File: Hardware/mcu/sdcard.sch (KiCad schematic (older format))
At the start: 2 parts, among them U801 MICROSD

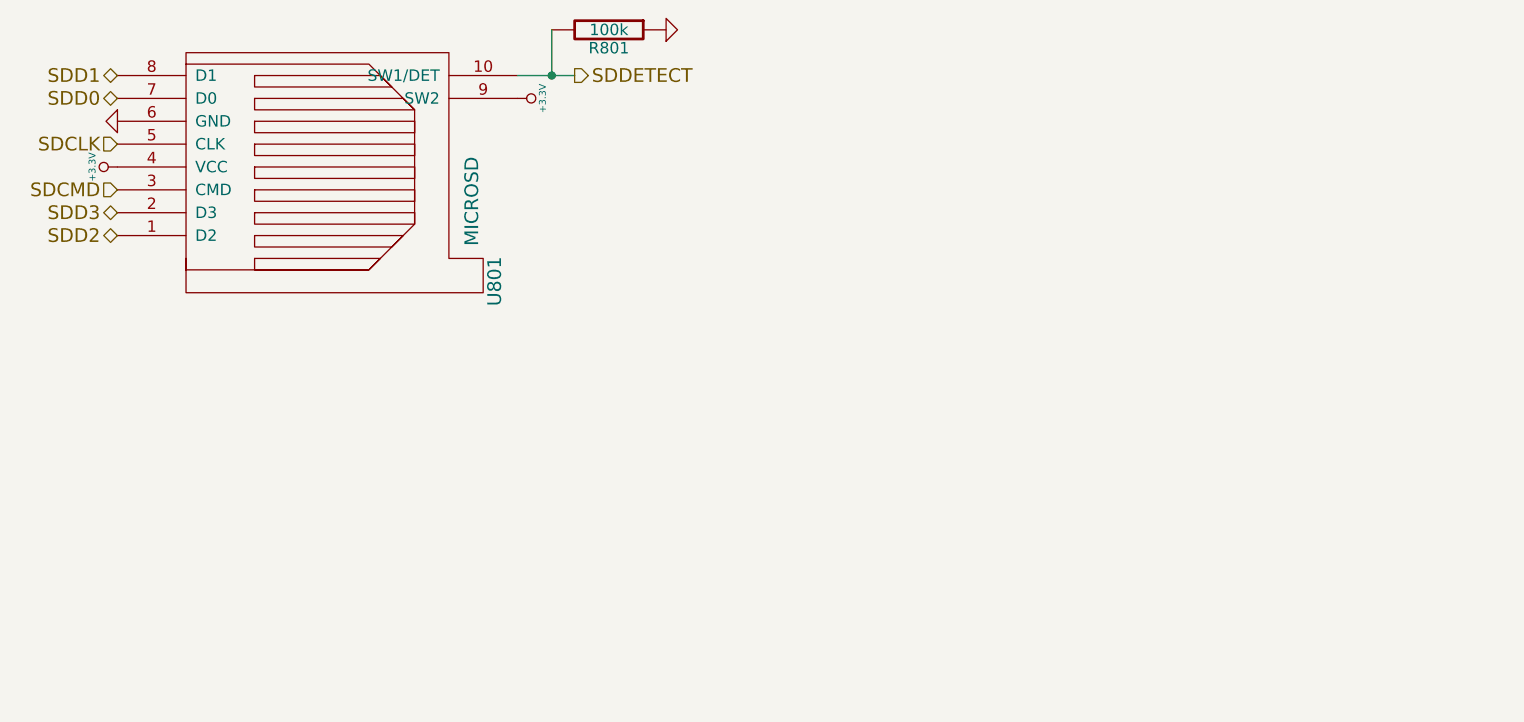
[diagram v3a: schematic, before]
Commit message: changes to mcu, new format and using a display adapter board
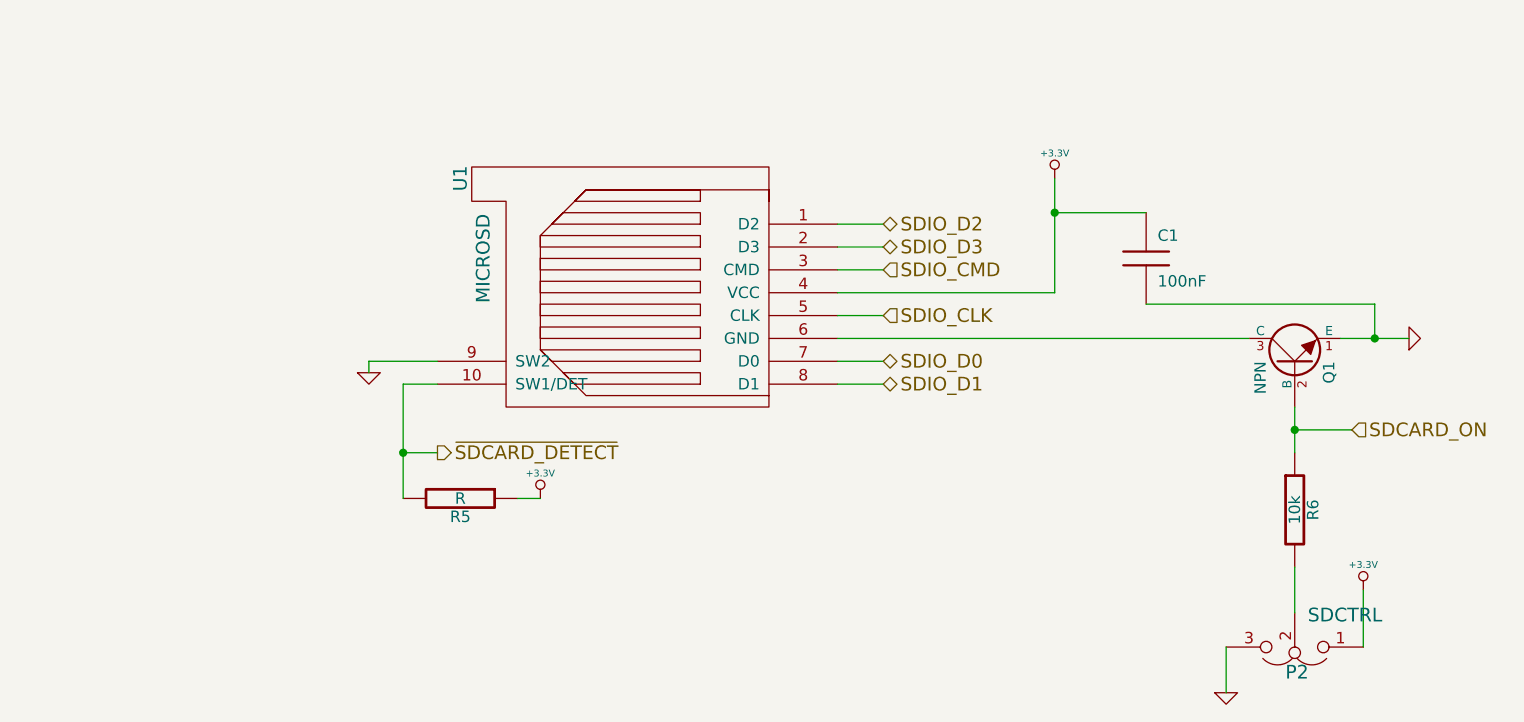
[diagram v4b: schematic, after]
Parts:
- removed R801: 100k, symbol R
- removed U801: MICROSD, symbol MICROSD
- added C1: 100nF, symbol C
- added P2: SDCTRL, symbol JUMPER3
- added Q1: NPN, symbol NPN
- added R5: R, symbol R
- added R6: 10k, symbol R
- added U1: MICROSD, symbol MICROSD
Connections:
- net +3.3V: now also C1.1, P2.1, R5.1, U1.4 (VCC)
- net GND: now also C1.2, P2.3, Q1.1 (E), U1.9 (SW2)
- new net: Q1.3 (C), U1.6 (GND)
- new net: P2.2, R6.2
- new net SDCARD_ON: Q1.2 (B), R6.1
- new net SDIO_CLK: U1.5 (CLK)
- new net SDIO_CMD: U1.3 (CMD)
- new net SDIO_D0: U1.7 (D0)
- new net SDIO_D1: U1.8 (D1)
- new net SDIO_D2: U1.1 (D2)
- new net SDIO_D3: U1.2 (D3)
- new net ~SDCARD_DETECT: R5.2, U1.10 (SW1/DET)
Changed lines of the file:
@@
-EESchema Schematic File Version 2  date Di 17 Mai 2011 02:16:23 CEST
+EESchema Schematic File Version 2  date So 17 Jul 2011 02:24:16 CEST
 LIBS:power
 LIBS:device
@@
 LIBS:valves
 LIBS:nhesse
-LIBS:bordcomputer-cache
+LIBS:mcu-cache
 EELAYER 25  0
 EELAYER END
 $Descr A4 11700 8267
 encoding utf-8
-Sheet 8 9
+Sheet 4 9
 Title ""
-Date "17 may 2011"
+Date "16 jul 2011"
 Rev ""
 Comp ""
@@
 Comment4 ""
 $EndDescr
-$Comp
-L +3.3V #PWR036
-U 1 1 4D7434A2
-P 1150 1450
-F 0 "#PWR036" H 1150 1410 30  0001 C CNN
-F 1 "+3.3V" H 1150 1560 30  0000 C CNN
-	1    1150 1450
+Wire Wire Line
+	6300 3400 6300 3200
+Wire Wire Line
+	6000 3750 6000 3550
+Connection ~ 6300 2600
+Wire Wire Line
+	6300 2700 6300 2500
+Connection ~ 6650 2200
+Wire Wire Line
+	6650 2200 6650 2050
+Wire Wire Line
+	6650 2050 5650 2050
+Wire Wire Line
+	5250 1500 5250 2000
+Wire Wire Line
+	5250 2000 4300 2000
+Wire Wire Line
+	6800 2200 6500 2200
+Wire Wire Line
+	4500 2400 4300 2400
+Wire Wire Line
+	4500 2300 4300 2300
+Wire Wire Line
+	4500 2100 4300 2100
+Wire Wire Line
+	4500 1900 4300 1900
+Wire Wire Line
+	4500 1800 4300 1800
+Wire Wire Line
+	4500 1700 4300 1700
+Connection ~ 2400 2700
+Wire Wire Line
+	2400 2900 2400 2400
+Wire Wire Line
+	2400 2400 2550 2400
+Wire Wire Line
+	2400 2700 2550 2700
+Wire Wire Line
+	2250 2350 2250 2300
+Wire Wire Line
+	2250 2300 2550 2300
+Wire Wire Line
+	3000 2900 2900 2900
+Wire Wire Line
+	6100 2200 4300 2200
+Wire Wire Line
+	5250 1650 5650 1650
+Connection ~ 5250 1650
+Wire Wire Line
+	6300 2600 6550 2600
+Wire Wire Line
+	6600 3300 6600 3550
+$Comp
+L +3.3V #PWR09
+U 1 1 4E175875
+P 6600 3300
+F 0 "#PWR09" H 6600 3260 30  0001 C CNN
+F 1 "+3.3V" H 6600 3410 30  0000 C CNN
+	1    6600 3300
+	1    0    0    -1
+$EndComp
+$Comp
+L JUMPER3 P2
+U 1 1 4E17586A
+P 6300 3550
+F 0 "P2" H 6290 3660 60  0000 C CNN
+F 1 "SDCTRL" H 6080 3410 60  0000 C CNN
+	1    6300 3550
+	-1   0    0    1
+$EndComp
+$Comp
+L GND #PWR010
+U 1 1 4E175822
+P 6000 3750
+F 0 "#PWR010" H 6000 3750 30  0001 C CNN
+F 1 "GND" H 6000 3680 30  0001 C CNN
+	1    6000 3750
+	1    0    0    -1
+$EndComp
+Text HLabel 6550 2600 2    60   Input ~ 0
+SDCARD_ON
+$Comp
+L R R6
+U 1 1 4E175812
+P 6300 2950
+F 0 "R6" V 6380 2950 50  0000 C CNN
+F 1 "10k" V 6300 2950 50  0000 C CNN
+	1    6300 2950
+	1    0    0    -1
+$EndComp
+$Comp
+L C C1
+U 1 1 4E1757FC
+P 5650 1850
+F 0 "C1" H 5700 1950 50  0000 L CNN
+F 1 "100nF" H 5700 1750 50  0000 L CNN
+	1    5650 1850
+	1    0    0    -1
+$EndComp
+$Comp
+L +3.3V #PWR011
+U 1 1 4E1757ED
+P 5250 1500
+F 0 "#PWR011" H 5250 1460 30  0001 C CNN
+F 1 "+3.3V" H 5250 1610 30  0000 C CNN
+	1    5250 1500
+	1    0    0    -1
+$EndComp
+$Comp
+L GND #PWR012
+U 1 1 4E1757D1
+P 6800 2200
+F 0 "#PWR012" H 6800 2200 30  0001 C CNN
+F 1 "GND" H 6800 2130 30  0001 C CNN
+	1    6800 2200
 	0    -1   -1   0
 $EndComp
 $Comp
-L GND #PWR037
-U 1 1 4D7434A0
-P 1150 1250
-F 0 "#PWR037" H 1150 1250 30  0001 C CNN
-F 1 "GND" H 1150 1180 30  0001 C CNN
-	1    1150 1250
+L NPN Q1
+U 1 1 4E1757BB
+P 6300 2300
+F 0 "Q1" H 6300 2150 50  0000 R CNN
+F 1 "NPN" H 6300 2450 50  0000 R CNN
+	1    6300 2300
+	0    -1   -1   0
+$EndComp
+$Comp
+L +3.3V #PWR013
+U 1 1 4E175794
+P 3000 2900
+F 0 "#PWR013" H 3000 2860 30  0001 C CNN
+F 1 "+3.3V" H 3000 3010 30  0000 C CNN
+	1    3000 2900
+	1    0    0    -1
+$EndComp
+$Comp
+L R R5
+U 1 1 4E175778
+P 2650 2900
+F 0 "R5" V 2730 2900 50  0000 C CNN
+F 1 "R" V 2650 2900 50  0000 C CNN
+	1    2650 2900
 	0    1    1    0
 $EndComp
-Text HLabel 1150 1750 0    60   BiDi ~ 0
-SDD2
-Text HLabel 1150 1650 0    60   BiDi ~ 0
-SDD3
-Text HLabel 1150 1550 0    60   Input ~ 0
-SDCMD
-Text HLabel 1150 1350 0    60   Input ~ 0
-SDCLK
-Text HLabel 1150 1150 0    60   BiDi ~ 0
-SDD0
-Text HLabel 1150 1050 0    60   BiDi ~ 0
-SDD1
-Connection ~ 3050 1050
-Wire Wire Line
-	3050 850  3050 1050
-Wire Wire Line
-	2900 1050 3150 1050
-$Comp
-L GND #PWR038
-U 1 1 4D743467
-P 3550 850
-F 0 "#PWR038" H 3550 850 30  0001 C CNN
-F 1 "GND" H 3550 780 30  0001 C CNN
-	1    3550 850
-	0    -1   -1   0
-$EndComp
-$Comp
-L R R801
-U 1 1 4D743462
-P 3300 850
-F 0 "R801" V 3380 850 50  0000 C CNN
-F 1 "100k" V 3300 850 50  0000 C CNN
-	1    3300 850
+$Comp
+L GND #PWR014
+U 1 1 4E175772
+P 2250 2350
+F 0 "#PWR014" H 2250 2350 30  0001 C CNN
+F 1 "GND" H 2250 2280 30  0001 C CNN
+	1    2250 2350
+	1    0    0    -1
+$EndComp
+Text HLabel 2550 2700 2    60   Output ~ 0
+~SDCARD_DETECT
+Text HLabel 4500 2400 2    60   BiDi ~ 0
+SDIO_D1
+Text HLabel 4500 2300 2    60   BiDi ~ 0
+SDIO_D0
+Text HLabel 4500 2100 2    60   Input ~ 0
+SDIO_CLK
+Text HLabel 4500 1900 2    60   Input ~ 0
+SDIO_CMD
+Text HLabel 4500 1800 2    60   BiDi ~ 0
+SDIO_D3
+Text HLabel 4500 1700 2    60   BiDi ~ 0
+SDIO_D2
+$Comp
+L MICROSD U1
+U 1 1 4E175724
+P 3450 2000
+F 0 "U1" H 2950 1200 60  0000 C CNN
+F 1 "MICROSD" H 3300 1300 60  0000 C CNN
+	1    3450 2000
 	0    1    1    0
 $EndComp
-Text HLabel 3150 1050 2    60   Output ~ 0
-SDDETECT
-$Comp
-L +3.3V #PWR039
-U 1 1 4D74344F
-P 2900 1150
-F 0 "#PWR039" H 2900 1110 30  0001 C CNN
-F 1 "+3.3V" H 2900 1260 30  0000 C CNN
-	1    2900 1150
-	0    1    1    0
-$EndComp
-$Comp
-L MICROSD U801
-U 1 1 4D743442
-P 2000 1450
-F 0 "U801" H 1500 650 60  0000 C CNN
-F 1 "MICROSD" H 1850 750 60  0000 C CNN
-	1    2000 1450
-	0    -1   -1   0
-$EndComp
 $EndSCHEMATC
